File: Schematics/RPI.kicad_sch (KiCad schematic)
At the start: 14 parts, among them J1 RPi GPIO, J8 PWR, U4 24LC256

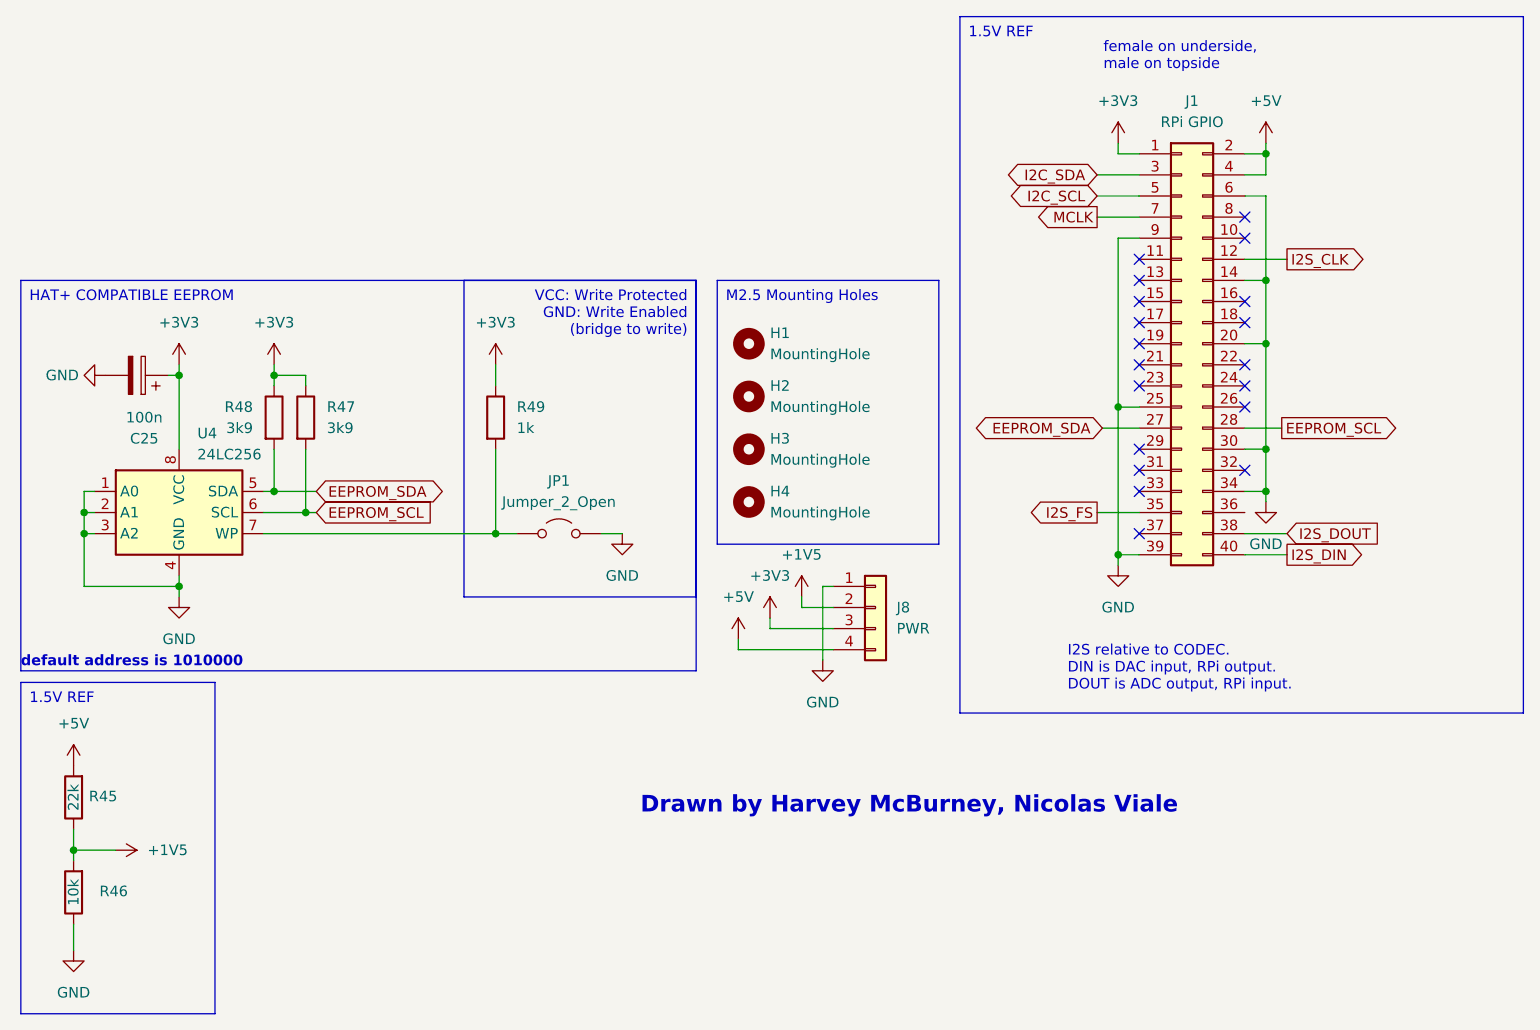
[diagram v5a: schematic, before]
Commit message: Started adding footprints, changed values.
Added footprints for most components. need to check in uni which sizes are available and what will need to be ordered from mouser.
Changed line in/out to TRS as this will be more reliable and added 0 ohm resistor options to bypass mono input and use line in/out as stereo.
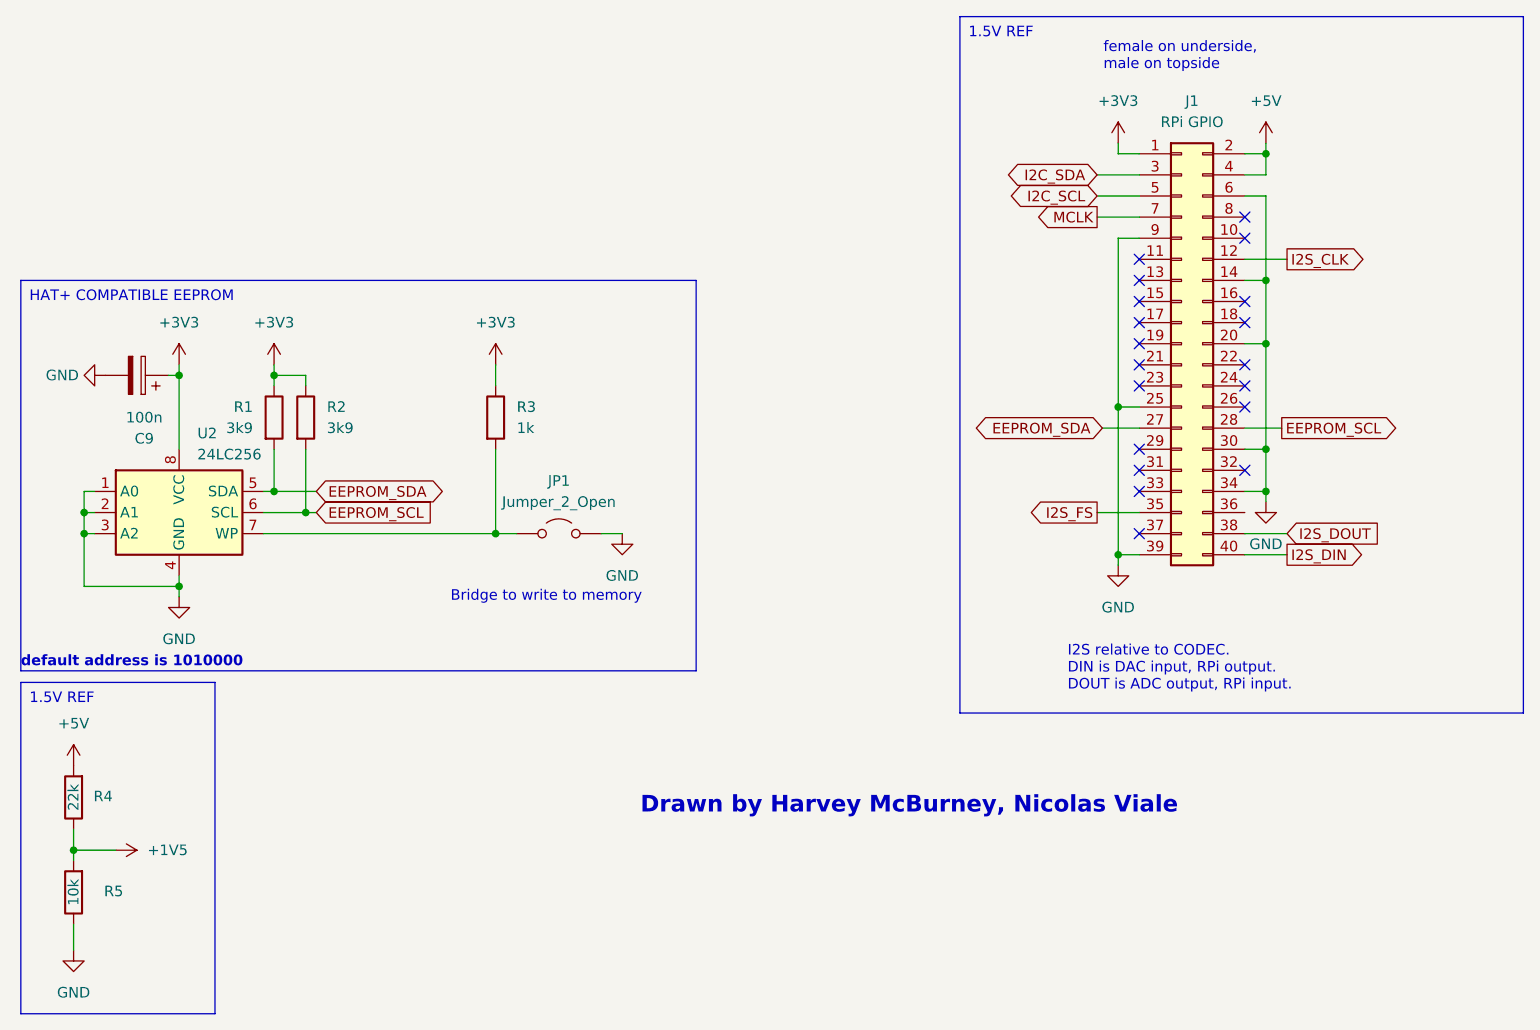
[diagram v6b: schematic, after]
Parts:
- removed H1, H2, H3, H4: MountingHole, symbol Mechanical:MountingHole
- removed J8: PWR, symbol Connector_Generic:Conn_01x04
- J1: footprint (none) -> Connector_PinHeader_2.54mm:PinHeader_2x20_P2.54mm_Vertical
- JP1: footprint (none) -> Connector_PinHeader_2.54mm:PinHeader_1x02_P2.54mm_Vertical
- R1: renamed from R48; footprint (none) -> Resistor_SMD:R_0603_1608Metric_Pad0.98x0.95mm_HandSolder
- R2: renamed from R47; footprint (none) -> Resistor_SMD:R_0603_1608Metric_Pad0.98x0.95mm_HandSolder
- R3: renamed from R49; footprint (none) -> Resistor_SMD:R_0603_1608Metric_Pad0.98x0.95mm_HandSolder
- R4: renamed from R45; footprint (none) -> Resistor_SMD:R_0603_1608Metric_Pad0.98x0.95mm_HandSolder
- R5: renamed from R46; footprint (none) -> Resistor_SMD:R_0603_1608Metric_Pad0.98x0.95mm_HandSolder
- U2: renamed from U4; footprint (none) -> Package_DIP:DIP-8_W7.62mm_Socket
- renumbered C25 to C9
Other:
- note added: "Bridge to write to memory"

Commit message: Updated to KiCAD v9
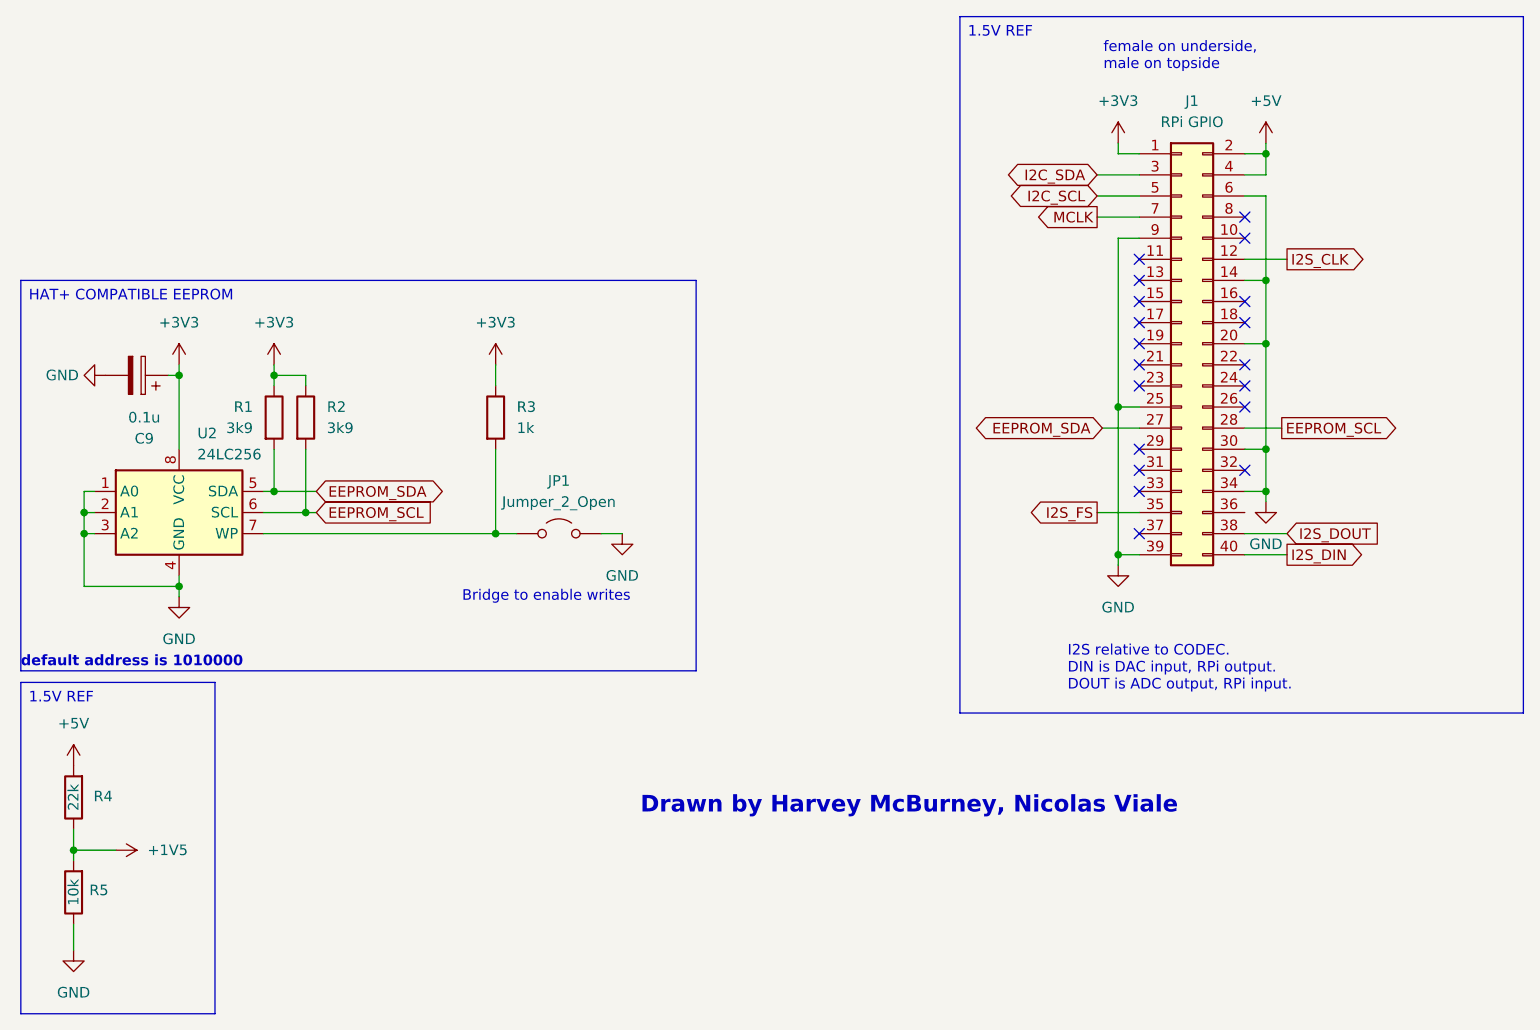
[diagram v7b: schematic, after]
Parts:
- C9: value 100n -> 0.1u
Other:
- note added: "Bridge to enable writes"
- note removed: "Bridge to write to memory"
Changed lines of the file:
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@@
 (kicad_sch
-	(version 20231120)
+	(version 20250114)
 	(generator "eeschema")
-	(generator_version "8.0")
+	(generator_version "9.0")
 	(paper "A5")
 	(title_block
@@
 		(date "2025-02-12")
 	)
+	(text "Drawn by Harvey McBurney, Nicolas Viale"
+		(exclude_from_sim no)
+		(at 123.444 107.696 0)
+		(effects
+			(font
+				(size 2 2)
+				(thickness 0.6)
+				(bold yes)
+			)
+		)
+	)
+	(text "female on underside,\nmale on topside"
+		(exclude_from_sim no)
+		(at 146.812 17.526 0)
+		(effects
+			(font
+				(size 1.27 1.27)
+			)
+			(justify left)
+		)
+	)
+	(text "default address is 1010000"
+		(exclude_from_sim no)
+		(at 16.51 90.424 0)
+		(effects
+			(font
+				(size 1.27 1.27)
+				(bold yes)
+			)
+			(justify left)
+		)
+	)
+	(text "I2S relative to CODEC.\nDIN is DAC input, RPi output.\nDOUT is ADC output, RPi input."
+		(exclude_from_sim no)
+		(at 142.494 91.186 0)
+		(effects
+			(font
+				(size 1.27 1.27)
+			)
+			(justify left)
+		)
+	)
+	(text "Bridge to enable writes"
+		(exclude_from_sim no)
+		(at 79.756 82.55 0)
+		(effects
+			(font
+				(size 1.27 1.27)
+			)
+		)
+	)
+	(text_box "1.5V REF"
+		(exclude_from_sim no)
+		(at 16.51 92.837 0)
+		(size 23.368 39.878)
+		(margins 0.9525 0.9525 0.9525 0.9525)
+		(stroke
+			(width 0)
+			(type default)
+		)
+		(fill
+			(type none)
+		)
+		(effects
+			(font
+				(size 1.27 1.27)
+			)
+			(justify left top)
+		)
+	)
+	(text_box "HAT+ COMPATIBLE EEPROM"
+		(exclude_from_sim no)
+		(at 16.51 44.45 0)
+		(size 81.28 46.99)
+		(margins 0.9525 0.9525 0.9525 0.9525)
+		(stroke
+			(width 0)
+			(type default)
+		)
+		(fill
+			(type none)
+		)
+		(effects
+			(font
+				(size 1.27 1.27)
+			)
+			(justify left top)
+		)
+	)
+	(text_box "1.5V REF"
+		(exclude_from_sim no)
+		(at 129.54 12.7 0)
+		(size 67.818 83.82)
+		(margins 0.9525 0.9525 0.9525 0.9525)
+		(stroke
+			(width 0)
+			(type default)
+		)
+		(fill
+			(type none)
+		)
+		(effects
+			(font
+				(size 1.27 1.27)
+			)
+			(justify left top)
+		)
+	)
 	(junction
 		(at 46.99 55.88)
@@
 			"kIAEJCABCUhAAhKQgAQkIAEJSEACEpCABCQgAQlIQAISkIAEJCABCUhAAhKQwAIRUCi5QJNlVyUg"
 			"AQlIQAISkIAEJCABCUhAAhKQgAQkIAEJSEACEpCABCQgAQlIQAISkIAEJCABCUhAAhKoR+D/AZnO"
-			"uPRlGhjBAAAAAElFTkSuQmCC"
+			"uPRlGhjBAAAAAElFTkSuQmCCZAA3AC8AegBXADUAWABwAFgAVwBVAEQATgBtADIANAAzAFIAVABW"
+			"AFEAdAA1AGUASgBKAHEAQQBCAFMAQwBnAEcAYwBDAEwAaQA4ADEAegAwAE8AZwB1AFoASQBUAFMA"
+			"QQBvAEgAZgAvAC8AOQA5ADUAdgBoAHcANABkAG4ASAB2AGwAOQA5ADkAMABYAGYAUgBUAEYAUgBW"
+			"AEcAMwA1AEYAaQBTAFIAaABSAFoATQBSADcAUgA4AGUAUwBUAFQANAA1AHUAeQB5AHIAZAA5AGIA"
+			"TABMAEwAbAB2ADMAbQAwAEwAOQBKADAAWAA2AHEAdgBXAFQAMQBWAEYAUwBOADUAcAAxAFkARgBv"
+			"AFQARwBlAGoARgBaAHMAQwBBAEEAVQAyAEgAcgBnADgASQAzAFIASwBMAEcAKwBNAFUAVgBUAE4A"
+			"KwAwACsAMgBjAGMAOAA0AHgAZQArAHkAeABSADEAMAA3AHUAbQBXAG4AQwBKAGIATgBSAEkANgBZ"
+			"AE8AcgBSADQAKwBPAEcASAA2ADgAWgBGAHQASgBzADAAVAAxAFAANABNAGgAegBLAGgAbQBkAGMA"
+			"NQBSADUAQwA3AGkAbABwAHUAWQBUAFcAeAAwAFAAdAArAGEAMwBtAHAAOABqAEMAYwBTAGQAMgBm"
+			"AGMAUABJAHUAYQBXAFYAUQAzADYAcgBkAHYAVwA3AEQAcQA2ADEAZAB2AEYAOQB0ADEAWQB2AEgA"
+			"cwBVAHMAVABWAHUAVQBxAFEAWQBCAGQATwBWAHEAcgBKAE8AUABVAFkAYgA4ADEAbgBkAHgAMwB2"
+			"AEUAeABKADEALwA3AFYAagB0ADEAVgBhAFgAVwAxAGkAVwB0AFIAcQBtADEATgBTAGYAdAA2AHgA"
+			"ZABkAGQASgBIAFoAWgBKAE4ATgBvAGwAUwB4AHMAbABQAFYASgBPADQAWQByADgAaQAvACsAagBj"
+			"AGMARgB6AHMAUwBXAGkAUABPADAAdAAyAG4AbgBuAHIAcQB6AFAAcQA1AHIAMwBXAGoASABYADgA"
+			"RQAwAE0AbgA5AHMAUwB4ADcAUwB5ADUANwBiAFEAVgBxAEEAcwBvAEEAQQBDAEEAQQBTAFUAUgBC"
+			"AFYARgBIADYAYQBpAHUAVwBjAGwAUwBSAGIAcgBuAGoAagBqAHMAMgBMAGEAcQBMAHAANABxADIA"
+			"cQBJAHUAcwBkAHMAcABWAFIAWAByADAAawBXADEAQwB0AGcAcQA5AEIAKwBKAFMAaQAxAEkAVwA4"
+			"AG4AdABDADAAZABpAFUANABTAFIAdQBTADIAbAAxAG8ASQA2AGoAWgBLAHMAbgBxADcAcQAvAG8A"
+			"NQBOAFgAZAArADEAYQBqAA=="
 		)
 	)
@@
 			"BIgAEQgKAiTgQdkp+kkEiAARIAJGCJCAG8EUmEEk4IHZKjpKBIgAESACBgiQgBuAxCFEgAgQASIQ"
 			"HARIwIOzVyaekoCboMQxRIAIEAEiEBQESMCDslP0kwgQASJABIwQIAE3gikwg0jAA7NVdJQIEAEi"
-			"QAQMEPh//GRkJJ3L/qcAAAAASUVORK5CYII="
-		)
-	)
-	(text_box "1.5V REF"
-		(exclude_from_sim no)
-		(at 16.51 92.837 0)
-		(size 23.368 39.878)
-		(stroke
-			(width 0)
-			(type default)
-		)
-		(fill
-			(type none)
-		)
-		(effects
-			(font
-				(size 1.27 1.27)
-			)
-			(justify left top)
-		)
-	)
-	(text_box "HAT+ COMPATIBLE EEPROM"
-		(exclude_from_sim no)
-		(at 16.51 44.45 0)
-		(size 81.28 46.99)
-		(stroke
-			(width 0)
-			(type default)
-		)
-		(fill
-			(type none)
-		)
-		(effects
-			(font
-				(size 1.27 1.27)
-			)
-			(justify left top)
-		)
-	)
-	(text_box "1.5V REF"
-		(exclude_from_sim no)
-		(at 129.54 12.7 0)
-		(size 67.818 83.82)
-		(stroke
-			(width 0)
-			(type default)
-		)
-		(fill
-			(type none)
-		)
-		(effects
-			(font
-				(size 1.27 1.27)
-			)
-			(justify left top)
-		)
-	)
-	(text "Drawn by Harvey McBurney, Nicolas Viale"
-		(exclude_from_sim no)
-		(at 123.444 107.696 0)
-		(effects
-			(font
-				(size 2 2)
-				(thickness 0.6)
-				(bold yes)
-			)
-		)
-	)
-	(text "female on underside,\nmale on topside"
-		(exclude_from_sim no)
-		(at 146.812 17.526 0)
-		(effects
-			(font
-				(size 1.27 1.27)
-			)
-			(justify left)
-		)
-	)
-	(text "default address is 1010000"
-		(exclude_from_sim no)
-		(at 16.51 90.424 0)
-		(effects
-			(font
-				(size 1.27 1.27)
-				(bold yes)
-			)
-			(justify left)
-		)
-	)
-	(text "I2S relative to CODEC.\nDIN is DAC input, RPi output.\nDOUT is ADC output, RPi input."
-		(exclude_from_sim no)
-		(at 142.494 91.186 0)
-		(effects
-			(font
-				(size 1.27 1.27)
-			)
-			(justify left)
-		)
-	)
-	(text "Bridge to write to memory"
-		(exclude_from_sim no)
-		(at 79.756 82.55 0)
-		(effects
-			(font
-				(size 1.27 1.27)
-			)
+			"QAQMEPh//GRkJJ3L/qcAAAAASUVORK5CYIJVAHkAUQB5AEMAWABaAHMAMgBhAFMAWAArADcALwAv"
+			"ADcANwB4AGMAQwBCAEEAMwBOACsATQAyAHQAbABrAHIASQBuAGkAdQA4AFAAZgBJAGUAWQBEAGQA"
+			"OABIAE8AQQBnAEcAUABsAGgAdgBCAC8ATgBaAHMAMgBhAEoAZgB2ADMANgA1AFkAeQBKADMAYQBG"
+			"AGIAUAB1AEgASgBKADYARABqAGsAMQBNAG8AbQBmAHoAbgBJAHIAWQA5AGYAUABUAFIAUgB3AFUA"
+			"VwBZAEsAegAyADYAYQBlAGYAaQBpAFoATgBtAHUAVAA4AHYAWQA1AFEAYwB1AGYATwBuAFEASwBU"
+			"AG4ATQB5AFEASQBzAFMAOABjAEsAOQBhAGcASABJAFMAMwAxAGoAcgBoAGsAaABFAE4AcQBIAEsA"
+			"UgBDADEASQBqAGUAagBYAHMASABBAGwATwA5AFYAcQBqAGsAWgBqAHYAawBkAG0ANAA4AEwAdgBm"
+			"AFgAawA5AEMAZgBnAGwAbwBEAE8AcAArAGIAMABuAHIALwBkAEcASQBBAGkAaAA1AFAAYgB0ADIA"
+			"NAAzAG8AZwBuAGIAcAB0AHYAdgAwADYAUwBPAFEARAB0AHIATgBRAHIAeABxADcAbwBCADQAVQBy"
+			"AGEAZwBuAGUAawB4AFQAbQB3AGgAaABMADcAVgBuAG4AegB5AHkAUgB6AG4AMwBCAHMAbABZAFQA"
+			"agB2AHEAcABTAEcARQBEAHQAaQBYAG4AQQB6AFYAMgB6AGUAdgBGAGwAYQBEAHcAUwBPAFAAWAB2"
+			"ADIAegBLAG8AQwBRAHAAOAB2AHYALwB6AFMAYQAxAE4AWgBQAGkAVQBFAHUAQwBrAGIANwA0AEUA"
+			"TwBVAGkAagBwAFIAQQBLAHAAVAB5AEUATwBsAEoAawBxAFMAaQAvAEsASQBnAEoAbAAwADYAWgBO"
+			"AHAAUQBMAEwAVABGADEANAA1ADcAWgBwADAAOABhAHAAQwBiADUAKwA5ADcAcABSAGkAcABQAEEA"
+			"MQBwAE8AbgBFAEUAawBpAHkAbwB6AFYASQBNAGoAQgB4AGcARABTAHgANQBvAE4ANABpAE0AcwBz"
+			"AE4ASgBJAEkARwB3AEMAOQBKAFgARABKAGgAeQAvACsAcgBHADIAQQBaAEUAawBJAGcARwByAHIA"
+			"RQBXAEwARgBtAEwASwBsAEMAbABLAGMAVQB3AFEAdgBaADQANgBkAGEAcQA0ACsATwBLAEwAcABW"
+			"AFYAaABqAFMATwB6AFAAbgBIAFMAUwBTAGQASgB2AHcASABzAGgASgBMAG8AbwArAHIAZwBGAEYA"
+			"TABDAHEAZwBSAEIAYgB2AHYAbABkAFYATw=="
 		)
 	)
@@
 	)
 	(symbol
+		(lib_id "Jumper:Jumper_2_Open")
+		(at 81.28 74.93 0)
+		(unit 1)
+		(exclude_from_sim yes)
+		(in_bom yes)
+		(on_board yes)
+		(dnp no)
+		(fields_autoplaced yes)
+		(property "Reference" "JP1"
+			(at 81.28 68.58 0)
+			(effects
+				(font
+					(size 1.27 1.27)
+				)
+			)
+		)
+		(property "Value" "Jumper_2_Open"
+			(at 81.28 71.12 0)
+			(effects
+				(font
+					(size 1.27 1.27)
+				)
+			)
+		)
+		(property "Footprint" "Connector_PinHeader_2.54mm:PinHeader_1x02_P2.54mm_Vertical"
+			(at 81.28 74.93 0)
+			(effects
+				(font
+					(size 1.27 1.27)
+				)
+				(hide yes)
+			)
+		)
+		(property "Datasheet" "~"
+			(at 81.28 74.93 0)
+			(effects
+				(font
+					(size 1.27 1.27)
+				)
+				(hide yes)
+			)
+		)
+		(property "Description" "Jumper, 2-pole, open"
+			(at 81.28 74.93 0)
+			(effects
+				(font
+					(size 1.27 1.27)
+				)
+				(hide yes)
+			)
+		)
+		(pin "1"
+		)
+		(pin "2"
+		)
+		(instances
+			(project ""
+				(path "/41751dd2-97f9-4cc6-b9e6-b561e5949053/94150540-adfd-4870-80d6-c5485bc02207"
+					(reference "JP1")
+					(unit 1)
+				)
+			)
+		)
+	)
+	(symbol
 		(lib_id "Device:C_Polarized")
 		(at 30.48 55.88 270)
@@
 			)
 		)
-		(property "Value" "100n"
+		(property "Value" "0.1u"
 			(at 31.369 60.96 90)
 			(effects
@@
 		(dnp no)
 		(property "Reference" "R5"
-			(at 27.686 117.983 0)
+			(at 25.908 117.856 0)
 			(effects
 				(font
@@
 					(unit 1)
 				)
-			)
-		)
-	)
-	(symbol
-		(lib_id "Jumper:Jumper_2_Open")
-		(at 81.28 74.93 0)
-		(unit 1)
-		(exclude_from_sim yes)
-		(in_bom yes)
-		(on_board yes)
-		(dnp no)
-		(fields_autoplaced yes)
-		(property "Reference" "JP1"
-			(at 81.28 68.58 0)
-			(effects
-				(font
-					(size 1.27 1.27)
-				)
-			)
-		)
-		(property "Value" "Jumper_2_Open"
-			(at 81.28 71.12 0)
-			(effects
-				(font
-					(size 1.27 1.27)
-				)
-			)
-		)
-		(property "Footprint" "Connector_PinHeader_2.54mm:PinHeader_1x02_P2.54mm_Vertical"
-			(at 81.28 74.93 0)
-			(effects
-				(font
-					(size 1.27 1.27)
-				)
-				(hide yes)
-			)
-		)
-		(property "Datasheet" "~"
-			(at 81.28 74.93 0)
-			(effects
-				(font
-					(size 1.27 1.27)
-				)
-				(hide yes)
-			)
-		)
-		(property "Description" "Jumper, 2-pole, open"
-			(at 81.28 74.93 0)
-			(effects
-				(font
-					(size 1.27 1.27)
-				)
-				(hide yes)
-			)
-		)
-		(pin "1"
-		)
-		(pin "2"
-		)
-		(instances
-			(project ""
-				(path "/41751dd2-97f9-4cc6-b9e6-b561e5949053/94150540-adfd-4870-80d6-c5485bc02207"
-					(reference "JP1")
-					(unit 1)
-				)
